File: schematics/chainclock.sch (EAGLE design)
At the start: 23 parts, among them SW1 ROTARTY_ENCODER

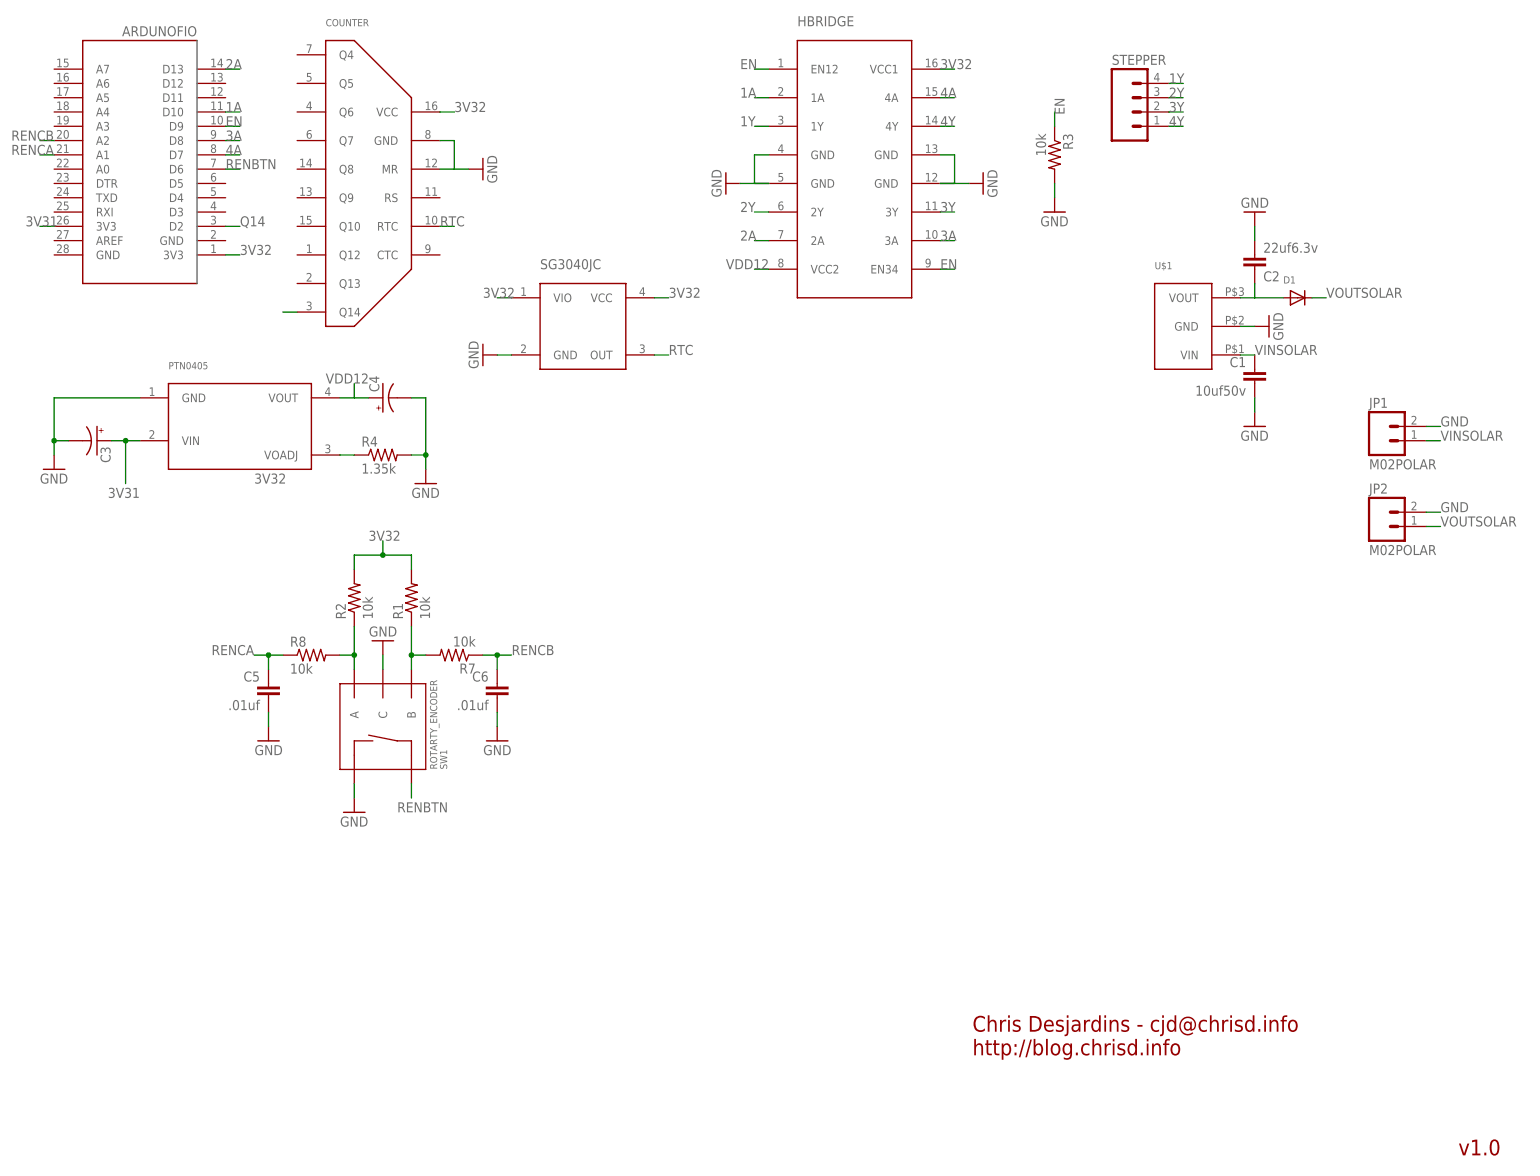
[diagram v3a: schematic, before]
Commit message: Updated to use 2 4060 and...
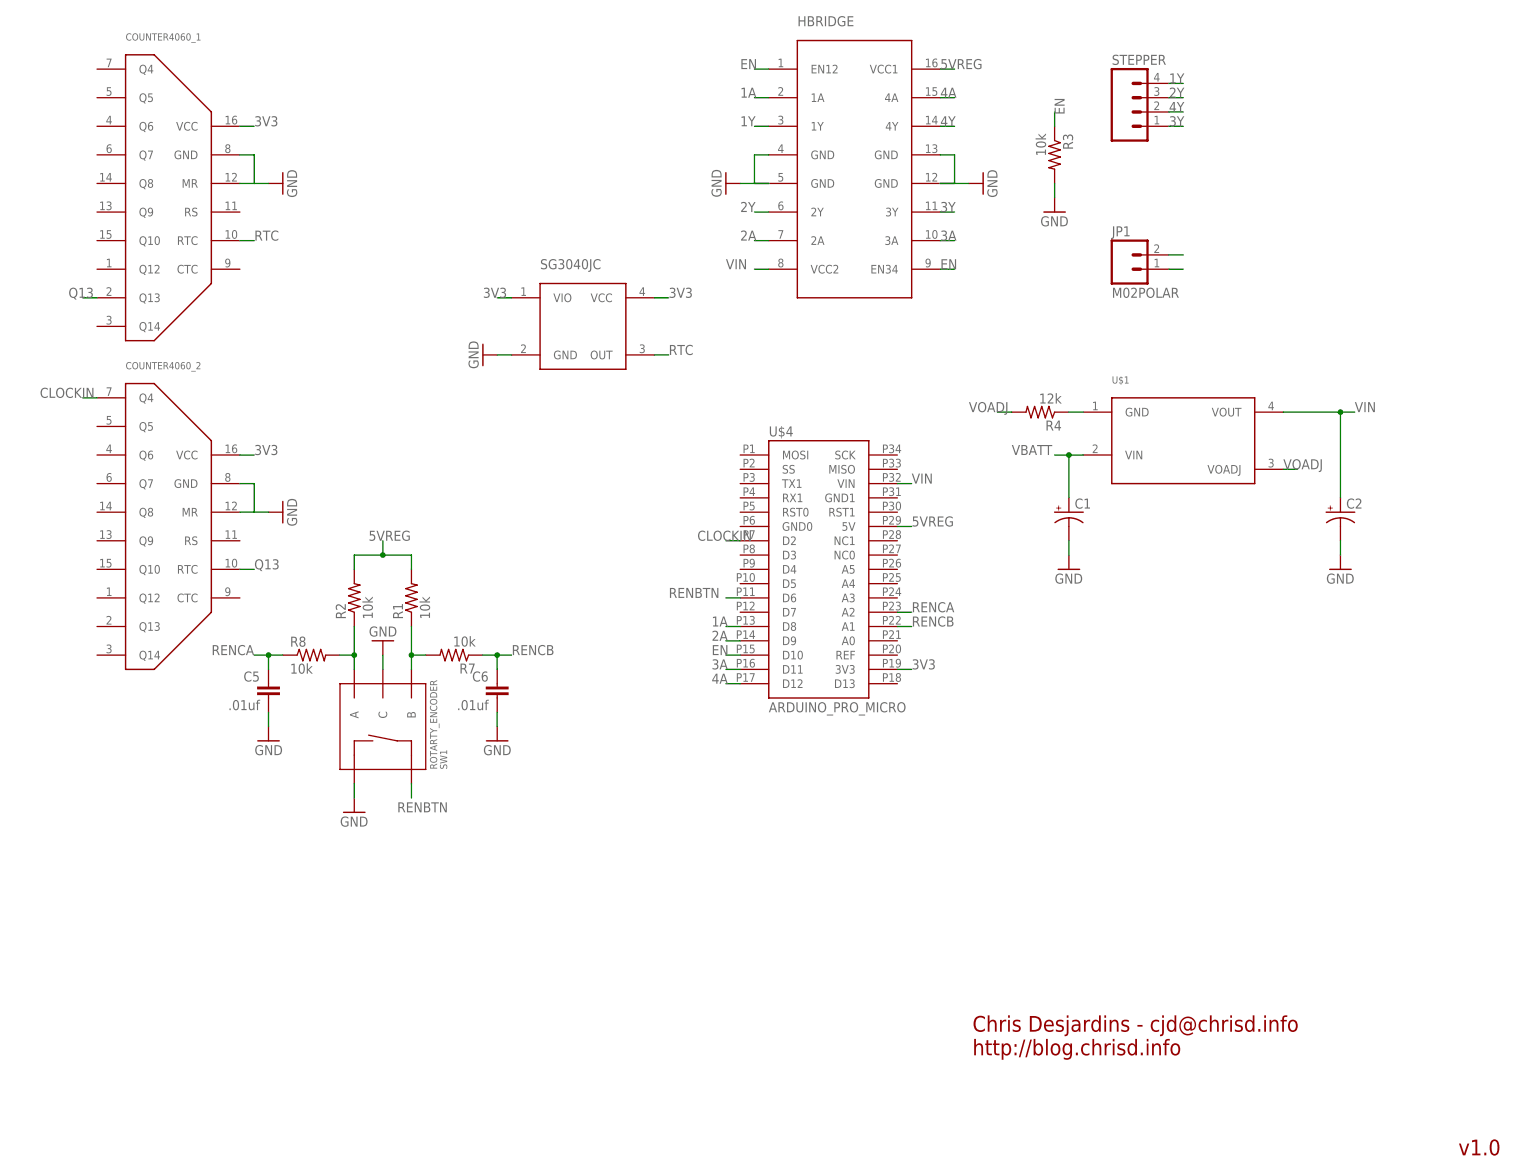
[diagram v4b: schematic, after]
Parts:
- removed ARDUNOFIO: ARDUINOFIO, desjardins:ARDUINOFIO
- removed C3, C4: (no value), SparkFun-Passives:CAP_POLPTH1
- removed COUNTER: 4060, desjardins:4060
- removed D1: (no value), adafruit:DIODEDO-1N4148
- removed JP2: M02POLAR, desjardins:M02POLAR
- removed PTN0405: PTN0405C, desjardins:PTN0405C
- added COUNTER4060_1, COUNTER4060_2: 4060SOIC16, desjardins:4060SOIC16
- added U$4: ARDUINO_PRO_MICRO, ChrisD:ARDUINO_PRO_MICRO
- C1: value 10uf50v -> (none); device SparkFun-Capacitors:CAPKIT -> SparkFun-Capacitors:CAP_POLPTH1
- C2: value 22uf6.3v -> (none); device SparkFun-Capacitors:CAPKIT -> SparkFun-Capacitors:CAP_POLPTH1
- R4: value 1.35k -> 12k
- U$1: value V78-500 -> PTN0405C; device desjardins:V78-500 -> desjardins:PTN0405C
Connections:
- removed net 3V31: ARDUNOFIO.3V3@1, C3.+, PTN0405.VIN
- removed net 3V32: ARDUNOFIO.3V3@0, COUNTER.VCC, HBRIDGE.VCC1, R1.2, R2.2, SG3040JC.VCC, SG3040JC.VIO
- removed net N$3: PTN0405.VOADJ, R4.1
- removed net N$4: C2.1, D1.A, U$1.VOUT
- removed net Q14: ARDUNOFIO.D2, COUNTER.Q14
- removed net VDD12: C4.+, HBRIDGE.VCC2, PTN0405.VOUT
- removed net VINSOLAR: C1.1, JP1.1, U$1.VIN
- removed net VOUTSOLAR: D1.C, JP2.1
- new net 3V3: COUNTER4060_1.VCC, COUNTER4060_2.VCC, SG3040JC.VCC, SG3040JC.VIO, U$4.3V3
- new net 5VREG: HBRIDGE.VCC1, R1.2, R2.2, U$4.5V
- new net CLOCKIN: COUNTER4060_2.Q4, U$4.D2
- new net N$1: R4.1, U$1.GND
- new net Q13: COUNTER4060_1.Q13, COUNTER4060_2.RTC
- new net VBATT: C1.+, JP1.1, U$1.VIN
- new net VIN: C2.+, HBRIDGE.VCC2, U$1.VOUT, U$4.VIN
- new net VOADJ: R4.2, U$1.VOADJ
- net 1A: now also U$4.D8; no longer ARDUNOFIO.D10
- net 2A: now also U$4.D9; no longer ARDUNOFIO.D13
- net 3A: now also U$4.D11; no longer ARDUNOFIO.D8
- net 3Y: now also STEPPER.1; no longer STEPPER.2
- net 4A: now also U$4.D12; no longer ARDUNOFIO.D7
- net 4Y: now also STEPPER.2; no longer STEPPER.1
- net EN: now also U$4.D10; no longer ARDUNOFIO.D9
- net GND: now also C1.-, C2.-, COUNTER4060_1.GND, COUNTER4060_1.MR, COUNTER4060_2.GND, COUNTER4060_2.MR; no longer C1.2, C2.2, C3.-, C4.-, COUNTER.GND, COUNTER.MR, JP2.2, PTN0405.GND, R4.2, U$1.GND
- net RENBTN: now also U$4.D6; no longer ARDUNOFIO.D6
- net RENCA: now also U$4.A2; no longer ARDUNOFIO.A1
- net RENCB: now also U$4.A1; no longer ARDUNOFIO.A2
- net RTC: now also COUNTER4060_1.RTC; no longer COUNTER.RTC
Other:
- moved on the sheet: JP1, R4

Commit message: Use int line for rot enc
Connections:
- net RENCA: now also U$4.D3; no longer U$4.A2
- net RENCB: now also U$4.D4; no longer U$4.A1
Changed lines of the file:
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@@
 <pinref part="U$4" gate="G$1" pin="D2"/>
 <wire x1="134.62" y1="116.84" x2="132.08" y2="116.84" width="0.1524" layer="91"/>
-<label x="127" y="116.84" size="1.778" layer="95"/>
+<label x="132.08" y="119.38" size="1.778" layer="95" rot="R180"/>
 </segment>
 <segment>
@@
 <pinref part="U$4" gate="G$1" pin="D10"/>
 <wire x1="134.62" y1="96.52" x2="132.08" y2="96.52" width="0.1524" layer="91"/>
-<label x="129.54" y="96.52" size="1.778" layer="95"/>
+<label x="132.08" y="99.06" size="1.778" layer="95" rot="R180"/>
 </segment>
 </net>
@@
 <pinref part="U$4" gate="G$1" pin="D8"/>
 <wire x1="134.62" y1="101.6" x2="132.08" y2="101.6" width="0.1524" layer="91"/>
-<label x="129.54" y="101.6" size="1.778" layer="95"/>
+<label x="132.08" y="104.14" size="1.778" layer="95" rot="R180"/>
 </segment>
 </net>
@@
 <pinref part="U$4" gate="G$1" pin="D12"/>
 <wire x1="134.62" y1="91.44" x2="132.08" y2="91.44" width="0.1524" layer="91"/>
-<label x="129.54" y="91.44" size="1.778" layer="95"/>
+<label x="132.08" y="93.98" size="1.778" layer="95" rot="R180"/>
 </segment>
 </net>
@@
 <pinref part="U$4" gate="G$1" pin="D11"/>
 <wire x1="134.62" y1="93.98" x2="132.08" y2="93.98" width="0.1524" layer="91"/>
-<label x="129.54" y="93.98" size="1.778" layer="95"/>
+<label x="132.08" y="96.52" size="1.778" layer="95" rot="R180"/>
 </segment>
 </net>
@@
 <pinref part="U$4" gate="G$1" pin="D9"/>
 <wire x1="134.62" y1="99.06" x2="132.08" y2="99.06" width="0.1524" layer="91"/>
-<label x="129.54" y="99.06" size="1.778" layer="95"/>
+<label x="132.08" y="101.6" size="1.778" layer="95" rot="R180"/>
 </segment>
 </net>
@@
 <pinref part="U$4" gate="G$1" pin="D6"/>
 <wire x1="134.62" y1="106.68" x2="132.08" y2="106.68" width="0.1524" layer="91"/>
-<label x="121.92" y="106.68" size="1.778" layer="95"/>
+<label x="132.08" y="109.22" size="1.778" layer="95" rot="R180"/>
 </segment>
 </net>
@@
 </segment>
 <segment>
-<pinref part="U$4" gate="G$1" pin="A1"/>
-<wire x1="162.56" y1="101.6" x2="165.1" y2="101.6" width="0.1524" layer="91"/>
-<label x="165.1" y="101.6" size="1.778" layer="95"/>
+<pinref part="U$4" gate="G$1" pin="D4"/>
+<wire x1="134.62" y1="111.76" x2="132.08" y2="111.76" width="0.1524" layer="91"/>
+<label x="132.08" y="114.3" size="1.778" layer="95" rot="R180"/>
 </segment>
 </net>
@@
 </segment>
 <segment>
-<pinref part="U$4" gate="G$1" pin="A2"/>
-<wire x1="162.56" y1="104.14" x2="165.1" y2="104.14" width="0.1524" layer="91"/>
-<label x="165.1" y="104.14" size="1.778" layer="95"/>
-</segment>
-</net>
+<pinref part="U$4" gate="G$1" pin="D3"/>
+<wire x1="134.62" y1="114.3" x2="132.08" y2="114.3" width="0.1524" layer="91"/>
+<label x="132.08" y="116.84" size="1.778" layer="95" rot="R180"/>
+</segment>
+</net>
